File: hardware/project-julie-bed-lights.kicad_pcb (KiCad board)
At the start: 2 copper layers, 57.2 x 22.9 mm, 4 parts, among them J1 2199230-4, J2 Conn_01x15_Female, J3 Conn_01x15_Female

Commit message: First placement
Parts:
- added C1: 10uF, Capacitor_SMD:C_1210_3225Metric_Pad1.33x2.70mm_HandSolder, F.Cu at (53.0, 123.0)
- added C2: 100nF, Capacitor_SMD:C_0603_1608Metric, F.Cu at (57.0, 116.0)
- added C3: 47pF, Capacitor_SMD:C_0603_1608Metric, F.Cu at (49.5, 116.0)
- added C4: 22uF, Capacitor_SMD:C_1210_3225Metric_Pad1.33x2.70mm_HandSolder, F.Cu at (59.0, 126.0)
- added C5: 22uF, Capacitor_SMD:C_1210_3225Metric_Pad1.33x2.70mm_HandSolder, F.Cu at (59.0, 123.0)
- added D1: LED, LED_SMD:LED_0603_1608Metric, F.Cu at (62.0, 135.0)
- added J4: Screw_Terminal_01x02, Conn_Molex_393570002:Molex-393570002-MFG, F.Cu at (52.0, 135.0)
- added L1: 6.8uH, SRP4020TA-6R8M:IND_SRP4020TA-6R8M, F.Cu at (61.0, 119.0)
- added Q1: IRF8736TRPBF‎, Package_SO:SOIC-8_3.9x4.9mm_P1.27mm, F.Cu at (84.0, 122.0)
- added Q2: IRF8736TRPBF‎, Package_SO:SOIC-8_3.9x4.9mm_P1.27mm, F.Cu at (91.6, 122.0)
- added Q3: IRF8736TRPBF‎, Package_SO:SOIC-8_3.9x4.9mm_P1.27mm, F.Cu at (99.2, 122.0)
- added R1: 10k, Resistor_SMD:R_0603_1608Metric, F.Cu at (84.8, 115.0)
- added R2: R_Small, Resistor_SMD:R_0603_1608Metric, F.Cu at (51.0, 116.0)
- added R3: R_Small, Resistor_SMD:R_0603_1608Metric, F.Cu at (54.0, 116.0)
- added R4: 10k, Resistor_SMD:R_0603_1608Metric, F.Cu at (92.4, 115.0)
- added R5: 10k, Resistor_SMD:R_0603_1608Metric, F.Cu at (100.0, 115.0)
- added R6: 10k, Resistor_SMD:R_0603_1608Metric, F.Cu at (60.0, 135.0)
- added SW1: SW_SPST, Button_Switch_SMD:SW_SPST_B3U-1000P, F.Cu at (63.0, 83.0)
- added U1: AP63300WU-7, AP63300WU-7:SOT95P280X100-6N, F.Cu at (55.0, 119.0)
- J2: value Conn_01x15_Female -> BM06B-SRSS-TB(LF)(SN); footprint Connector_PinHeader_2.54mm:PinHeader_1x15_P2.54mm_Vertical -> BM06B-SRSS-TB(LF)(SN):JST_BM06B-SRSS-TB(LF)(SN); moved to F.Cu
- J3: value Conn_01x15_Female -> Screw_Terminal_01x04; footprint Connector_PinHeader_2.54mm:PinHeader_1x15_P2.54mm_Vertical -> Conn_Molex_393570004:Molex-393570004-MFG; moved to F.Cu
- moved J3 42.2 mm to (96.0, 135.0), turned to 0 degrees
- moved J2 11.2 mm to (53.0, 83.0), turned to 0 degrees
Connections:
- J2 pad 1: +5V -> GND
- J2 pad 2: +5V -> /RTS
- J2 pad 3: GND -> /DTR
- J2 pad 4: /GPIO25-DAC1 -> /RX
- J2 pad 5: /GPIO26-DAC2 -> /TX
- J2 pad 6: /GPIO33 -> +5V
- J3 pad 1: GND -> +12V
- J3 pad 2: GND -> /RED
- J3 pad 3: GND -> /GREEN
- J3 pad 4: /GPIO18 -> /BLUE
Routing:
- net /DTR: track 45.4 -> 0.00 mm
- net /GPIO22: track 42.9 -> 0.00 mm, vias 2 -> 0
- net /RTS: track 42.7 -> 0.00 mm
- net /GPIO16: track 41.3 -> 0.00 mm, vias 2 -> 0
- net /GPIO21: track 40.0 -> 0.00 mm, vias 2 -> 0
- net /RX: track 39.9 -> 0.00 mm
- net /GPIO4: track 38.7 -> 0.00 mm, vias 2 -> 0
- net /TX: track 36.4 -> 0.00 mm
- net /GPIO2: track 33.2 -> 0.00 mm, vias 2 -> 0
- net /GPIO27: track 31.1 -> 0.00 mm, vias 2 -> 0
- net /RESET: track 29.2 -> 0.00 mm
- net /GPIO5: track 28.5 -> 0.00 mm
- net /GPIO15: track 27.5 -> 0.00 mm, vias 2 -> 0
- net /GPIO32: track 26.4 -> 0.00 mm
- net /GPIO26-DAC2: track 25.4 -> 0.00 mm, vias 2 -> 0
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- removed copper zone on F.Cu, net +5V
- removed copper zone on B.Cu, net GND
- removed copper zone on F.Cu, net GND

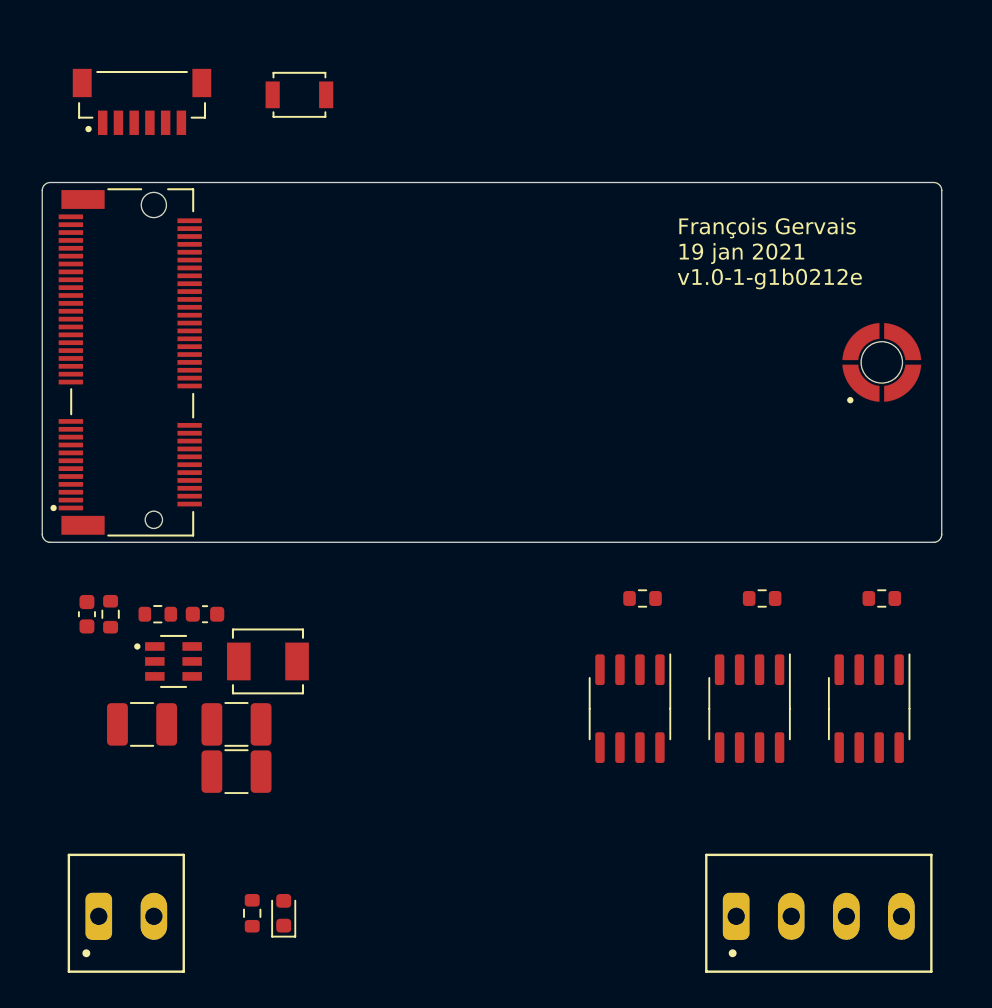
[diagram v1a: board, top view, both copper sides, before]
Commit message: DC-DC converter routing
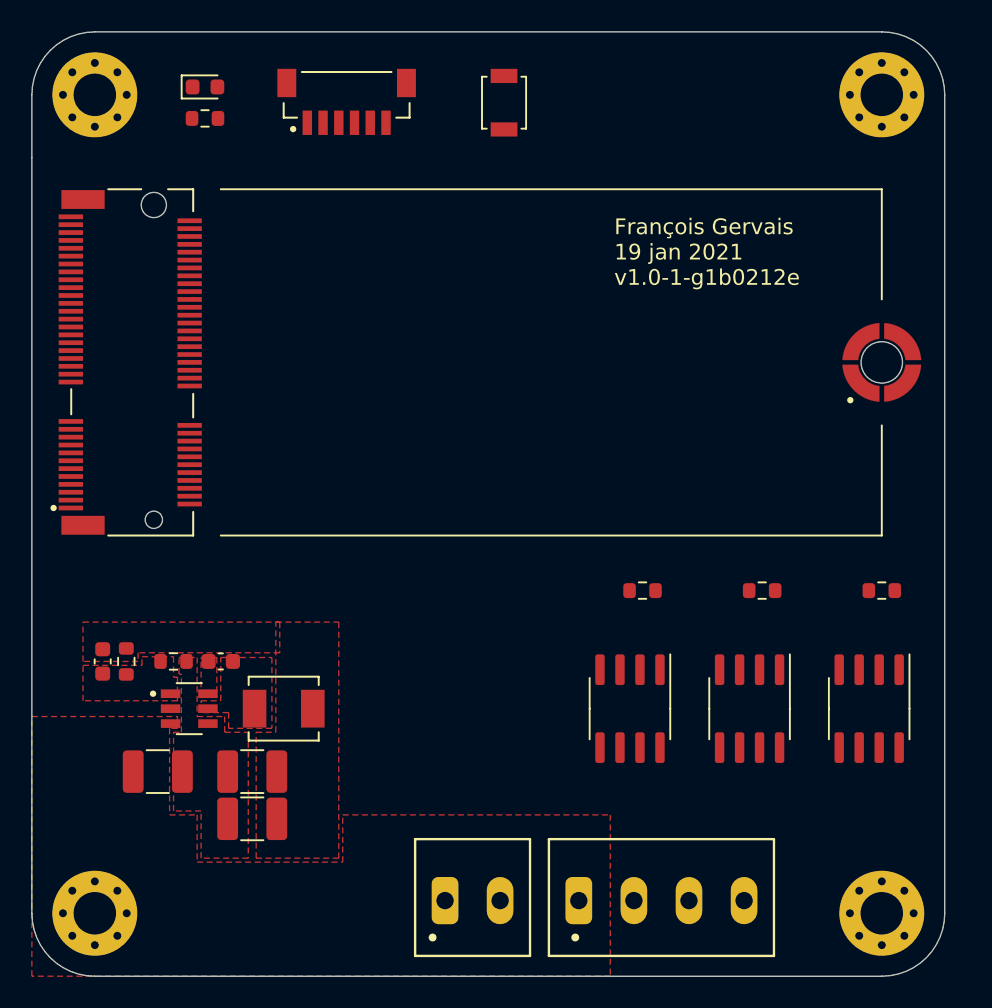
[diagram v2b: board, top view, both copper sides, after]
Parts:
- added REF**: MountingHole_2.7mm_M2.5_Pad_Via, MountingHole:MountingHole_2.7mm_M2.5_Pad_Via, F.Cu at (100.0, 135.0)
- added REF**: MountingHole_2.7mm_M2.5_Pad_Via, MountingHole:MountingHole_2.7mm_M2.5_Pad_Via, F.Cu at (50.0, 135.0)
- added REF**: MountingHole_2.7mm_M2.5_Pad_Via, MountingHole:MountingHole_2.7mm_M2.5_Pad_Via, F.Cu at (50.0, 83.0)
- added REF**: MountingHole_2.7mm_M2.5_Pad_Via, MountingHole:MountingHole_2.7mm_M2.5_Pad_Via, F.Cu at (100.0, 83.0)
- moved D1 52.7 mm to (57.0, 82.5), turned to 0 degrees
- moved R6 50.6 mm to (57.0, 84.5), turned to 180 degrees
- moved J4 22.0 mm to (74.0, 134.0)
- moved SW1 13.0 mm to (76.0, 83.5), turned to 90 degrees
- moved J2 13.0 mm to (66.0, 83.0)
- moved J3 10.0 mm to (86.0, 134.0)
- moved C1 3.16 mm to (54.0, 126.0)
- moved C2 3.16 mm to (58.0, 119.0)
- moved C3 3.16 mm to (50.5, 119.0)
- moved C4 3.16 mm to (60.0, 129.0)
- moved C5 3.16 mm to (60.0, 126.0)
- moved L1 3.16 mm to (62.0, 122.0)
- moved R2 3.16 mm to (52.0, 119.0)
- moved R3 3.16 mm to (55.0, 119.0)
- moved U1 3.16 mm to (56.0, 122.0)
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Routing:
- added copper zone on F.Cu, net +12V
- added copper zone on F.Cu, net +5V
- added copper zone on F.Cu, net GND
- added copper zone on F.Cu, net Net-(C2-Pad1)
- added copper zone on F.Cu, net Net-(C2-Pad2)
- added copper zone on F.Cu, net Net-(C3-Pad2)
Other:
- board size 57.2 x 22.9 mm -> 58 x 60 mm

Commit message: First routing except ground
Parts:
- moved SW1 13.0 mm to (63.0, 83.5)
- moved J2 7.00 mm to (73.0, 83.0)
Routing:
- net /GPIO5: track 0.00 -> 53.2 mm
- net /GPIO23: track 0.00 -> 46.9 mm
- net /GPIO19: track 0.00 -> 37.1 mm
- net /TX: track 0.00 -> 27.5 mm
- net /DTR: track 0.00 -> 27.0 mm
- net /RX: track 0.00 -> 25.1 mm
- net /RTS: track 0.00 -> 23.2 mm
- net /RESET: track 0.00 -> 15.2 mm
- net Net-(D1-Pad2): track 0.00 -> 2.02 mm
- added copper zone on F.Cu, net /BLUE
- added copper zone on F.Cu, net /GREEN
- added copper zone on F.Cu, net /RED
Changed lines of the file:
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@@
     (thickness 1.6)
     (drawings 17)
-    (tracks 0)
+    (tracks 43)
     (zones 0)
     (modules 27)
@@
   )
   (setup
-    (last_trace_width 0.1524)
+    (last_trace_width 0.25)
     (user_trace_width 0.1524)
     (trace_clearance 0.1524)
@@
   )
   (module Button_Switch_SMD:SW_SPST_B3U-1000P (layer F.Cu)
-    (at 76 83.5 90)
+    (at 63 83.5 90)
     (descr "Ultra-small-sized Tactile Switch with High Contact Reliability, Top-actuated Model, without Ground Terminal, without Boss")
     (tags "Tactile Switch")
@@
   )
   (module "BM06B-SRSS-TB(LF)(SN):JST_BM06B-SRSS-TB(LF)(SN)" (layer F.Cu)
-    (at 66 83)
+    (at 73 83)
     (fp_text reference J2 (at -1.905 -2.67) (layer F.SilkS) hide
       (effects (font (size 1 1) (thickness 0.015)))
@@
     )
   )
+  (gr_line (start 58 89) (end 100 89) (layer F.SilkS) (width 0.12))
   (gr_poly (pts (xy 56.5 122.5) (xy 58.5 122.5) (xy 58.5 124) (xy 60 124) (xy 60 131) (xy 54 131) (xy 54 124) (xy 55.5 124) (xy 55.5 120) (xy 55 120) (xy 55 118.5) (xy 56.5 118.5)) (layer Dwgs.User) (width 0.1))
   (gr_line (start 100 111) (end 100 104) (layer F.SilkS) (width 0.12))
   (gr_line (start 58 111) (end 100 111) (layer F.SilkS) (width 0.12))
   (gr_line (start 100 89) (end 100 96) (layer F.SilkS) (width 0.12))
-  (gr_line (start 58 89) (end 100 89) (layer F.SilkS) (width 0.12))
   (gr_arc (start 100 135) (end 100 139) (angle -90) (layer Edge.Cuts) (width 0.05))
   (gr_arc (start 50 135) (end 46 135) (angle -90) (layer Edge.Cuts) (width 0.05))
@@
     (effects (font (size 1 1) (thickness 0.15)) (justify left))
   )
+  (segment (start 63 90.949322) (end 56.949322 97) (width 0.25) (layer F.Cu) (net 42))
+  (segment (start 63 85.2) (end 63 90.949322) (width 0.25) (layer F.Cu) (net 42))
+  (segment (start 56.949322 97) (end 56.025 97) (width 0.25) (layer F.Cu) (net 42))
+  (segment (start 56.949322 100.5) (end 56.025 100.5) (width 0.25) (layer F.Cu) (net 45))
+  (segment (start 57.077401 100.371921) (end 56.949322 100.5) (width 0.25) (layer F.Cu) (net 45))
+  (segment (start 72.5 83.75) (end 72.25 83.5) (width 0.25) (layer F.Cu) (net 45))
+  (segment (start 72.5 84.775) (end 72.5 83.75) (width 0.25) (layer F.Cu) (net 45))
+  (segment (start 70 83.5) (end 68 85.5) (width 0.25) (layer F.Cu) (net 45))
+  (segment (start 68 85.5) (end 68 88.224661) (width 0.25) (layer F.Cu) (net 45))
+  (segment (start 57.077401 99.14726) (end 57.077401 100.371921) (width 0.25) (layer F.Cu) (net 45))
+  (segment (start 72.25 83.5) (end 70 83.5) (width 0.25) (layer F.Cu) (net 45))
+  (segment (start 68 88.224661) (end 57.077401 99.14726) (width 0.25) (layer F.Cu) (net 45))
+  (segment (start 71.5 84.775) (end 71.5 86.525) (width 0.25) (layer F.Cu) (net 46))
+  (segment (start 57.025 101) (end 56.025 101) (width 0.25) (layer F.Cu) (net 46))
+  (segment (start 71.5 86.525) (end 57.025 101) (width 0.25) (layer F.Cu) (net 46))
+  (segment (start 58 101.5) (end 56.025 101.5) (width 0.25) (layer F.Cu) (net 47))
+  (segment (start 73.5 84.775) (end 73.5 86) (width 0.25) (layer F.Cu) (net 47))
+  (segment (start 73.5 86) (end 58 101.5) (width 0.25) (layer F.Cu) (net 47))
+  (segment (start 57.0125 104) (end 56.025 104) (width 0.25) (layer F.Cu) (net 48))
+  (segment (start 74.5 84.775) (end 74.5 86.5125) (width 0.25) (layer F.Cu) (net 48))
+  (segment (start 74.5 86.5125) (end 57.0125 104) (width 0.25) (layer F.Cu) (net 48))
+  (segment (start 57.949322 105) (end 56.949322 106) (width 0.25) (layer F.Cu) (net 51))
+  (segment (start 56.949322 106) (end 56.025 106) (width 0.25) (layer F.Cu) (net 51))
+  (segment (start 88.5 105) (end 57.949322 105) (width 0.25) (layer F.Cu) (net 51))
+  (segment (start 97.295 119.525) (end 97.295 113.795) (width 0.25) (layer F.Cu) (net 51))
+  (segment (start 97.295 113.795) (end 88.5 105) (width 0.25) (layer F.Cu) (net 51))
+  (segment (start 98 114.5) (end 97.295 113.795) (width 0.25) (layer F.Cu) (net 51))
+  (segment (start 99.175 114.5) (end 98 114.5) (width 0.25) (layer F.Cu) (net 51))
+  (segment (start 57.949322 108) (end 56.949322 107) (width 0.25) (layer F.Cu) (net 55))
+  (segment (start 82.095 119.525) (end 70.57 108) (width 0.25) (layer F.Cu) (net 55))
+  (segment (start 56.949322 107) (end 56.025 107) (width 0.25) (layer F.Cu) (net 55))
+  (segment (start 70.57 108) (end 57.949322 108) (width 0.25) (layer F.Cu) (net 55))
+  (segment (start 82.095 116.38) (end 83.975 114.5) (width 0.25) (layer F.Cu) (net 55))
+  (segment (start 82.095 119.525) (end 82.095 116.38) (width 0.25) (layer F.Cu) (net 55))
+  (segment (start 89.695 119.525) (end 89.695 116.38) (width 0.25) (layer F.Cu) (net 56))
+  (segment (start 80.5 106.5) (end 56.025 106.5) (width 0.25) (layer F.Cu) (net 56))
+  (segment (start 89.695 115.695) (end 80.5 106.5) (width 0.25) (layer F.Cu) (net 56))
+  (segment (start 91.575 114.5) (end 91 114.5) (width 0.25) (layer F.Cu) (net 56))
+  (segment (start 91 114.5) (end 89.695 115.805) (width 0.25) (layer F.Cu) (net 56))
+  (segment (start 89.695 119.525) (end 89.695 115.805) (width 0.25) (layer F.Cu) (net 56))
+  (segment (start 89.695 115.805) (end 89.695 115.695) (width 0.25) (layer F.Cu) (net 56))
+  (segment (start 57.7875 84.4625) (end 57.825 84.5) (width 0.25) (layer F.Cu) (net 61))
+  (segment (start 57.7875 82.5) (end 57.7875 84.4625) (width 0.25) (layer F.Cu) (net 61))
   (zone (net 35) (net_name GND) (layer F.Cu) (hatch edge 0.508)
     (connect_pads (clearance 0.2))
@@
     (polygon
       (pts
-        (xy 61.75 118.45) (xy 52.75 118.45) (xy 52.75 119) (xy 49.25 119) (xy 49.25 116.5)
-        (xy 61.75 116.5)
+        (xy 62.5 91.5) (xy 57 97) (xy 57.028959 108.008145) (xy 65.5 108) (xy 65.5 118.45)
+        (xy 52.75 118.45) (xy 52.75 119) (xy 46 119) (xy 46 79) (xy 62.5 79)
       )
     )
+  )
+  (zone (net 64) (net_name /RED) (layer F.Cu) (hatch edge 0.508)
+    (connect_pads (clearance 0.2))
+    (min_thickness 0.254)
+    (fill yes (arc_segments 32) (thermal_gap 0.508) (thermal_bridge_width 0.508))
+    (polygon
+      (pts
+        (xy 87 128) (xy 86 128) (xy 86 139) (xy 83 139) (xy 83 128)
+        (xy 81 128) (xy 81 122.5) (xy 87 122.5)
+      )
+    )
+  )
+  (zone (net 63) (net_name /GREEN) (layer F.Cu) (hatch edge 0.508)
+    (connect_pads (clearance 0.2))
+    (min_thickness 0.254)
+    (fill yes (arc_segments 32) (thermal_gap 0.508) (thermal_bridge_width 0.508))
+    (polygon
+      (pts
+        (xy 95 130.5) (xy 89.5 130.5) (xy 89.5 139) (xy 86.5 139) (xy 86.5 129)
+        (xy 88 129) (xy 88 122.5) (xy 95 122.5)
+      )
+    )
+  )
+  (zone (net 62) (net_name /BLUE) (layer F.Cu) (hatch edge 0.508)
+    (connect_pads (clearance 0.2))
+    (min_thickness 0.254)
+    (fill yes (arc_segments 32) (thermal_gap 0.508) (thermal_bridge_width 0.508))
+    (polygon
+      (pts
+        (xy 104 139) (xy 90 139) (xy 90 131.5) (xy 96 131.5) (xy 96 122.5)
+        (xy 104 122.5)
+      )
+    )
+  )
+  (zone (net 35) (net_name GND) (layer F.Cu) (hatch edge 0.508)
+    (connect_pads (clearance 0.2))
+    (min_thickness 0.254)
+    (fill yes (arc_segments 32) (thermal_gap 0.508) (thermal_bridge_width 0.508))
+    (polygon
+      (pts
+        (xy 87 122) (xy 82.5 122) (xy 82.5 117) (xy 87 117)
+      )
+    )
+  )
+  (zone (net 35) (net_name GND) (layer F.Cu) (hatch edge 0.508)
+    (connect_pads (clearance 0.2))
+    (min_thickness 0.254)
+    (fill yes (arc_segments 32) (thermal_gap 0.508) (thermal_bridge_width 0.508))
+    (polygon
+      (pts
+        (xy 95 122) (xy 90 122) (xy 90 117) (xy 95 117)
+      )
+    )
+  )
+  (zone (net 35) (net_name GND) (layer F.Cu) (hatch edge 0.508)
+    (connect_pads (clearance 0.2))
+    (min_thickness 0.254)
+    (fill yes (arc_segments 32) (thermal_gap 0.508) (thermal_bridge_width 0.508))
+    (polygon
+      (pts
+        (xy 102.5 122) (xy 98 122) (xy 98 117) (xy 102.5 117)
+      )
+    )
+  )
+  (zone (net 36) (net_name +5V) (layer F.Cu) (hatch edge 0.508)
+    (connect_pads (clearance 0.2))
+    (min_thickness 0.254)
+    (fill yes (arc_segments 32) (thermal_gap 0.508) (thermal_bridge_width 0.508))
+    (polygon
+      (pts
+        (xy 80 86.5) (xy 69.5 86.5) (xy 69.5 91) (xy 60.5 91) (xy 60.5 79)
+        (xy 80 79)
+      )
+    )

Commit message: First routing
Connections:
- REF** pad 1: (no net) -> GND (x4)
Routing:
- net GND: track 0.00 -> 57.1 mm, vias 0 -> 59
- net +5V: track 0.00 -> 6.00 mm
- added copper zone on B.Cu, net GND
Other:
- board text added: "François Gervais 20 fev 2021 v"
- board text removed: "François Gervais 19 jan 2021 v1.0-1-g1b0212e"

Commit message: Add version of previous commit
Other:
- board text added: "François Gervais 20 fev 2021 v1.0"
- board text removed: "François Gervais 20 fev 2021 v"
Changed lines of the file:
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@@
   (gr_line (start 50 139) (end 100 139) (layer Edge.Cuts) (width 0.05))
   (gr_line (start 46 87) (end 46 135) (layer Edge.Cuts) (width 0.05))
-  (gr_text "François Gervais\n20 fev 2021\nv" (at 83 93) (layer F.SilkS)
+  (gr_text "François Gervais\n20 fev 2021\nv1.0" (at 83 93) (layer F.SilkS)
     (effects (font (size 1 1) (thickness 0.15)) (justify left))
   )

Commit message: Setup assembly print
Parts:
- R2: value R_Small -> 158k
- R3: value R_Small -> 30.1k

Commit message: Add polarity marking on power input
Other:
- board text added: "+"
